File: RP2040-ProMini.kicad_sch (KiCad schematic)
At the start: 33 parts, among them J1 CONN_L, J2 CONN_U, J3 CONN_R2, J4 CONN_R, Q1 AO3400A, U1 W25Q128JVS, U2 RP2040, U3 MIC5205-3.3YM5, Y1 12MHz

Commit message: Optimized few traces on PCB. Added few descriptive texts on schematics.
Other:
- note added: "LDO power supply"
- note added: "Main MCU"
- note added: "Main crystal"
- note added: "ProMini pin connectors"
- note added: "Pull-ups"
- note added: "QSPI Flash"
- note added: "Signalling LED"
- moved on the sheet: D1, JP1, Q1, R1
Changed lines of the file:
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@@
   (title_block
     (title "RP2040-ProMini-0010")
-    (date "2023-06-04")
+    (date "2023-06-09")
     (rev "1.0")
     (company "(c) 2023 Andriy Golovnya")
@@
     (stroke (width 0) (type default))
   )
-  (global_label "D13_SCK" (shape input) (at 60.96 133.35 180) (fields_autoplaced)
-    (effects (font (size 1.27 1.27)) (justify right))
-    (property "Intersheetrefs" "${INTERSHEET_REFS}" (at 49.6481 133.35 0)
+  (text "ProMini pin connectors" (at 217.17 30.48 0)
+    (effects (font (size 1.27 1.27)) (justify left bottom))
+  )
+  (text "Main MCU" (at 135.89 33.02 0)
+    (effects (font (size 1.27 1.27)) (justify left bottom))
+  )
+  (text "Main crystal" (at 53.34 82.55 0)
+    (effects (font (size 1.27 1.27)) (justify left bottom))
+  )
+  (text "Pull-ups" (at 224.79 90.17 0)
+    (effects (font (size 1.27 1.27)) (justify left bottom))
+  )
+  (text "Signalling LED" (at 54.61 111.76 0)
+    (effects (font (size 1.27 1.27)) (justify left bottom))
+  )
+  (text "LDO power supply" (at 220.98 120.65 0)
+    (effects (font (size 1.27 1.27)) (justify left bottom))
+  )
+  (text "QSPI Flash" (at 54.61 35.56 0)
+    (effects (font (size 1.27 1.27)) (justify left bottom))
+  )
+  (global_label "D13_SCK" (shape input) (at 59.69 143.51 180) (fields_autoplaced)
+    (effects (font (size 1.27 1.27)) (justify right))
+    (property "Intersheetrefs" "${INTERSHEET_REFS}" (at 48.3781 143.51 0)
       (effects (font (size 1.27 1.27)) (justify right) hide)
     )
@@
     )
   )
-  (symbol (lib_id "Device:R_Small") (at 68.58 118.11 0) (unit 1)
-    (in_bom yes) (on_board yes) (dnp no) (fields_autoplaced)
-    (property "Reference" "R1" (at 71.12 117.475 0)
-      (effects (font (size 1.27 1.27)) (justify left))
-    )
-    (property "Value" "10k" (at 71.12 120.015 0)
-      (effects (font (size 1.27 1.27)) (justify left))
-    )
-    (property "Footprint" "Resistor_SMD:R_0402_1005Metric" (at 68.58 118.11 0)
-      (effects (font (size 1.27 1.27)) hide)
-    )
-    (property "Datasheet" "~" (at 68.58 118.11 0)
+  (symbol (lib_id "Device:R_Small") (at 67.31 128.27 0) (unit 1)
+    (in_bom yes) (on_board yes) (dnp no) (fields_autoplaced)
+    (property "Reference" "R1" (at 69.85 127.635 0)
+      (effects (font (size 1.27 1.27)) (justify left))
+    )
+    (property "Value" "10k" (at 69.85 130.175 0)
+      (effects (font (size 1.27 1.27)) (justify left))
+    )
+    (property "Footprint" "Resistor_SMD:R_0402_1005Metric" (at 67.31 128.27 0)
+      (effects (font (size 1.27 1.27)) hide)
+    )
+    (property "Datasheet" "~" (at 67.31 128.27 0)
       (effects (font (size 1.27 1.27)) hide)
     )
@@
     )
   )
-  (symbol (lib_id "Device:LED_Small") (at 68.58 113.03 90) (unit 1)
-    (in_bom yes) (on_board yes) (dnp no) (fields_autoplaced)
-    (property "Reference" "D1" (at 71.12 112.3315 90)
+  (symbol (lib_id "Device:LED_Small") (at 67.31 123.19 90) (unit 1)
+    (in_bom yes) (on_board yes) (dnp no) (fields_autoplaced)
+    (property "Reference" "D1" (at 69.85 122.4915 90)
       (effects (font (size 1.27 1.27)) (justify right))
     )
-    (property "Value" "RED" (at 71.12 114.8715 90)
+    (property "Value" "RED" (at 69.85 125.0315 90)
       (effects (font (size 1.27 1.27)) (justify right))
     )
-    (property "Footprint" "LED_SMD:LED_0603_1608Metric" (at 68.58 113.03 90)
-      (effects (font (size 1.27 1.27)) hide)
-    )
-    (property "Datasheet" "~" (at 68.58 113.03 90)
+    (property "Footprint" "LED_SMD:LED_0603_1608Metric" (at 67.31 123.19 90)
+      (effects (font (size 1.27 1.27)) hide)
+    )
+    (property "Datasheet" "~" (at 67.31 123.19 90)
       (effects (font (size 1.27 1.27)) hide)
     )
@@
     )
   )
-  (symbol (lib_id "Jumper:SolderJumper_2_Bridged") (at 68.58 124.46 90) (unit 1)
-    (in_bom yes) (on_board yes) (dnp no) (fields_autoplaced)
-    (property "Reference" "JP1" (at 71.12 123.825 90)
+  (symbol (lib_id "Jumper:SolderJumper_2_Bridged") (at 67.31 134.62 90) (unit 1)
+    (in_bom yes) (on_board yes) (dnp no) (fields_autoplaced)
+    (property "Reference" "JP1" (at 69.85 133.985 90)
       (effects (font (size 1.27 1.27)) (justify right))
     )
-    (property "Value" "CUT_LED" (at 71.12 126.365 90)
+    (property "Value" "CUT_LED" (at 69.85 136.525 90)
       (effects (font (size 1.27 1.27)) (justify right))
     )
-    (property "Footprint" "Jumper:SolderJumper-2_P1.3mm_Bridged_RoundedPad1.0x1.5mm" (at 68.58 124.46 0)
-      (effects (font (size 1.27 1.27)) hide)
-    )
-    (property "Datasheet" "~" (at 68.58 124.46 0)
+    (property "Footprint" "Jumper:SolderJumper-2_P1.3mm_Bridged_RoundedPad1.0x1.5mm" (at 67.31 134.62 0)
+      (effects (font (size 1.27 1.27)) hide)
+    )
+    (property "Datasheet" "~" (at 67.31 134.62 0)
       (effects (font (size 1.27 1.27)) hide)
     )
@@
     )
   )
-  (symbol (lib_id "power:+3V3") (at 68.58 110.49 0) (unit 1)
-    (in_bom yes) (on_board yes) (dnp no) (fields_autoplaced)
-    (property "Reference" "#PWR07" (at 68.58 114.3 0)
-      (effects (font (size 1.27 1.27)) hide)
-    )
-    (property "Value" "+3V3" (at 68.58 106.68 0)
-      (effects (font (size 1.27 1.27)))
-    )
-    (property "Footprint" "" (at 68.58 110.49 0)
-      (effects (font (size 1.27 1.27)) hide)
-    )
-    (property "Datasheet" "" (at 68.58 110.49 0)
+  (symbol (lib_id "power:+3V3") (at 67.31 120.65 0) (unit 1)
+    (in_bom yes) (on_board yes) (dnp no) (fields_autoplaced)
+    (property "Reference" "#PWR07" (at 67.31 124.46 0)
+      (effects (font (size 1.27 1.27)) hide)
+    )
+    (property "Value" "+3V3" (at 67.31 116.84 0)
+      (effects (font (size 1.27 1.27)))
+    )
+    (property "Footprint" "" (at 67.31 120.65 0)
+      (effects (font (size 1.27 1.27)) hide)
+    )
+    (property "Datasheet" "" (at 67.31 120.65 0)
       (effects (font (size 1.27 1.27)) hide)
     )
@@
     )
   )
-  (symbol (lib_id "power:GND") (at 68.58 138.43 0) (unit 1)
-    (in_bom yes) (on_board yes) (dnp no) (fields_autoplaced)
-    (property "Reference" "#PWR08" (at 68.58 144.78 0)
-      (effects (font (size 1.27 1.27)) hide)
-    )
-    (property "Value" "GND" (at 68.58 143.51 0)
-      (effects (font (size 1.27 1.27)))
-    )
-    (property "Footprint" "" (at 68.58 138.43 0)
-      (effects (font (size 1.27 1.27)) hide)
-    )
-    (property "Datasheet" "" (at 68.58 138.43 0)
+  (symbol (lib_id "power:GND") (at 67.31 148.59 0) (unit 1)
+    (in_bom yes) (on_board yes) (dnp no) (fields_autoplaced)
+    (property "Reference" "#PWR08" (at 67.31 154.94 0)
+      (effects (font (size 1.27 1.27)) hide)
+    )
+    (property "Value" "GND" (at 67.31 153.67 0)
+      (effects (font (size 1.27 1.27)))
+    )
+    (property "Footprint" "" (at 67.31 148.59 0)
+      (effects (font (size 1.27 1.27)) hide)
+    )
+    (property "Datasheet" "" (at 67.31 148.59 0)
       (effects (font (size 1.27 1.27)) hide)
     )
@@
     )
   )
-  (symbol (lib_id "Transistor_FET:AO3400A") (at 66.04 133.35 0) (unit 1)
-    (in_bom yes) (on_board yes) (dnp no) (fields_autoplaced)
-    (property "Reference" "Q1" (at 72.39 132.715 0)
-      (effects (font (size 1.27 1.27)) (justify left))
-    )
-    (property "Value" "AO3400A" (at 72.39 135.255 0)
-      (effects (font (size 1.27 1.27)) (justify left))
-    )
-    (property "Footprint" "Package_TO_SOT_SMD:SOT-23" (at 71.12 135.255 0)
+  (symbol (lib_id "Transistor_FET:AO3400A") (at 64.77 143.51 0) (unit 1)
+    (in_bom yes) (on_board yes) (dnp no) (fields_autoplaced)
+    (property "Reference" "Q1" (at 71.12 142.875 0)
+      (effects (font (size 1.27 1.27)) (justify left))
+    )
+    (property "Value" "AO3400A" (at 71.12 145.415 0)
+      (effects (font (size 1.27 1.27)) (justify left))
+    )
+    (property "Footprint" "Package_TO_SOT_SMD:SOT-23" (at 69.85 145.415 0)
       (effects (font (size 1.27 1.27) italic) (justify left) hide)
     )
-    (property "Datasheet" "http://www.aosmd.com/pdfs/datasheet/AO3400A.pdf" (at 66.04 133.35 0)
-      (effects (font (size 1.27 1.27)) (justify left) hide)
-    )
+    (property "Datasheet" "http://www.aosmd.com/pdfs/datasheet/AO3400A.pdf" (at 64.77 143.51 0)
+      (effects (font (size 1.27 1.27)) (justify left) hide)
+    )

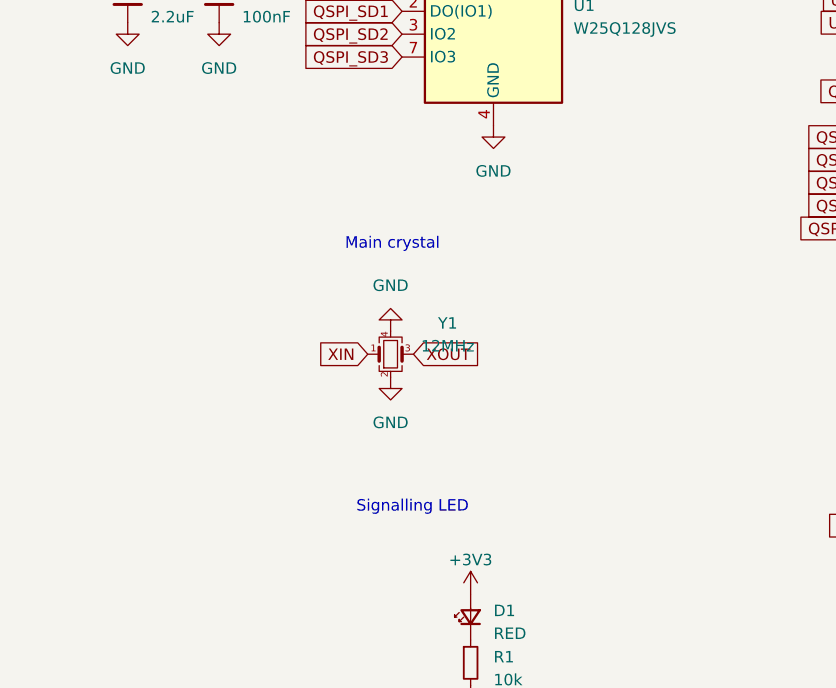
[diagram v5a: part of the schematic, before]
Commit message: Added alternative footprint for flash chip
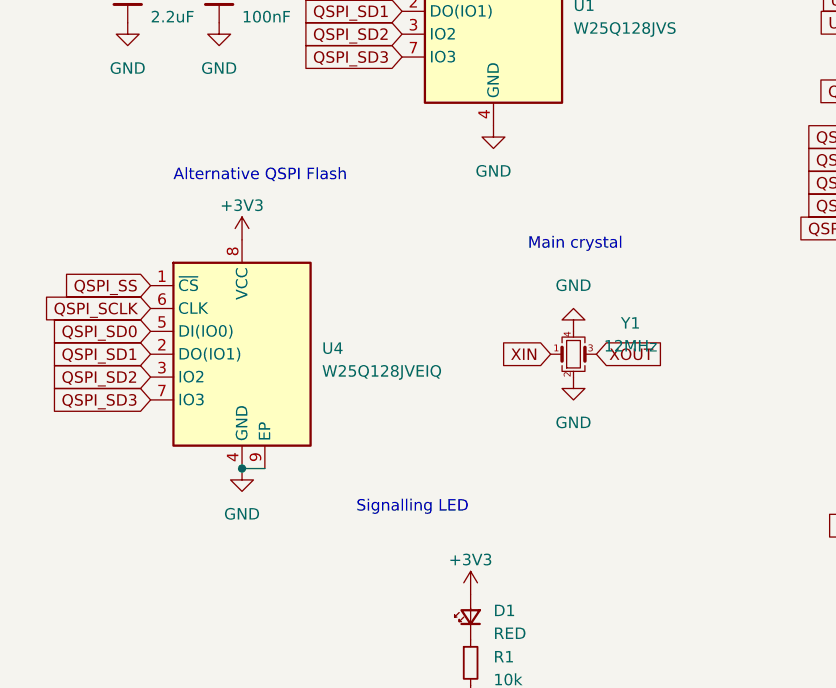
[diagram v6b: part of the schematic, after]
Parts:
- added U4: W25Q128JVEIQ, Package_SON:WSON-8-1EP_6x5mm_P1.27mm_EP3.4x4.3mm, symbol Memory_Flash:W25Q32JVZP
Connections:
- net +3V3: now also U4.8 (VCC)
- net GND: now also U4.4 (GND), U4.9 (EP)
- net QSPI_SCLK: now also U4.6 (CLK)
- net QSPI_SD0: now also U4.5 (DI(IO0))
- net QSPI_SD1: now also U4.2 (DO(IO1))
- net QSPI_SD2: now also U4.3 (IO2)
- net QSPI_SD3: now also U4.7 (IO3)
- net QSPI_SS: now also U4.1 (~{CS})
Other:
- note added: "Alternative QSPI Flash"
- moved on the sheet: Y1
